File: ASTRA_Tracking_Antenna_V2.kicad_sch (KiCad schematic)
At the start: 23 parts, among them J2 24V, J3 24V, J4 24V, J5 5V, J6 Conn_01x04_Socket, M1 Stepper Motor, U4 D24V22F3, U5 D24V22F5

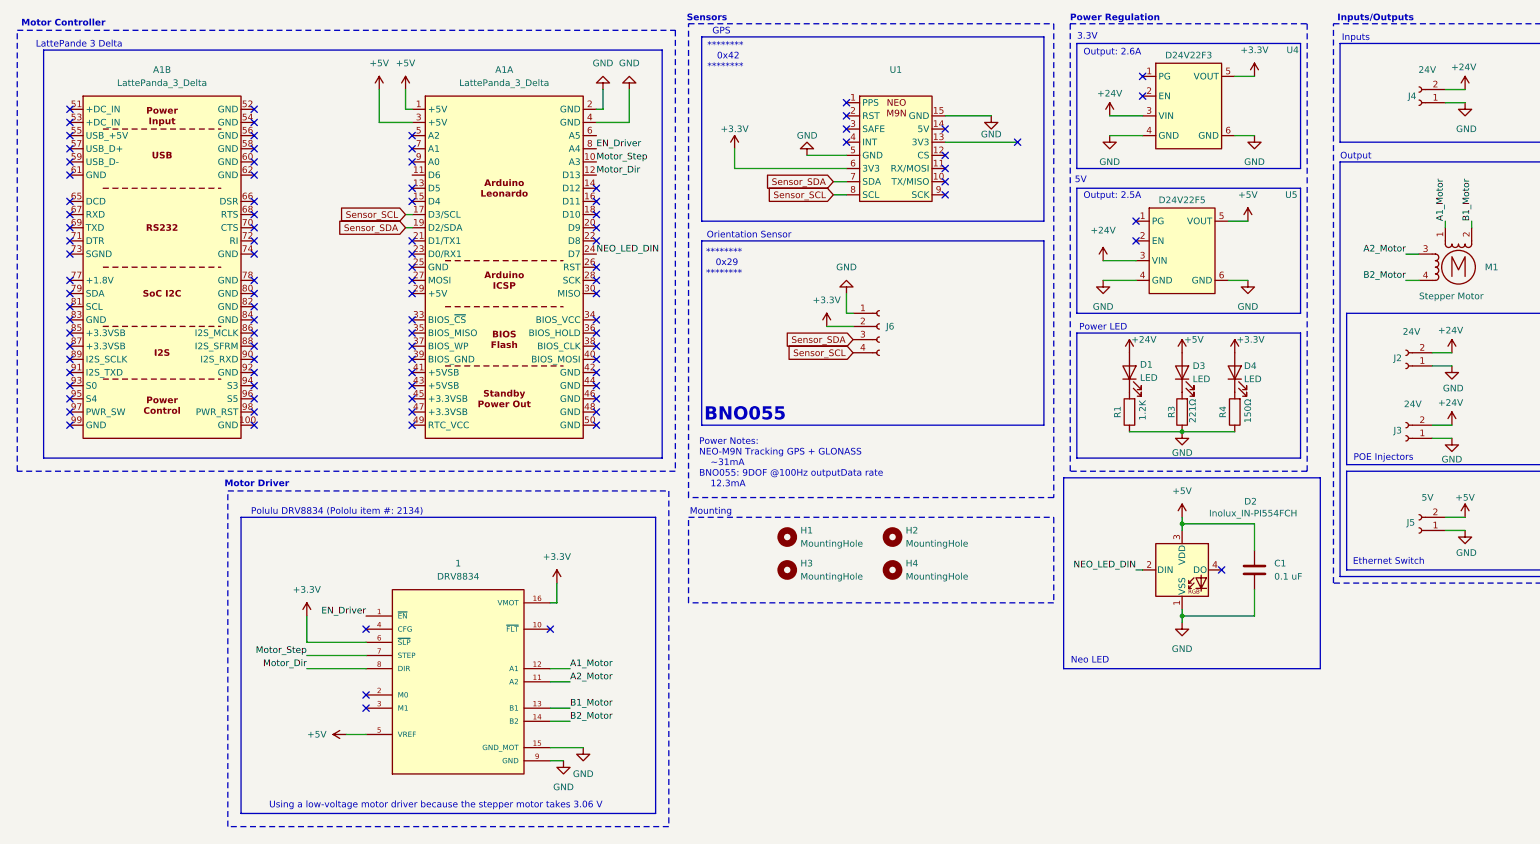
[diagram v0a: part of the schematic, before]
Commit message: PCB Created With SMD Driver
Tracking Antenna PCB revised to incorporate an SMD motor driver, and extraneous files also cleaned up.
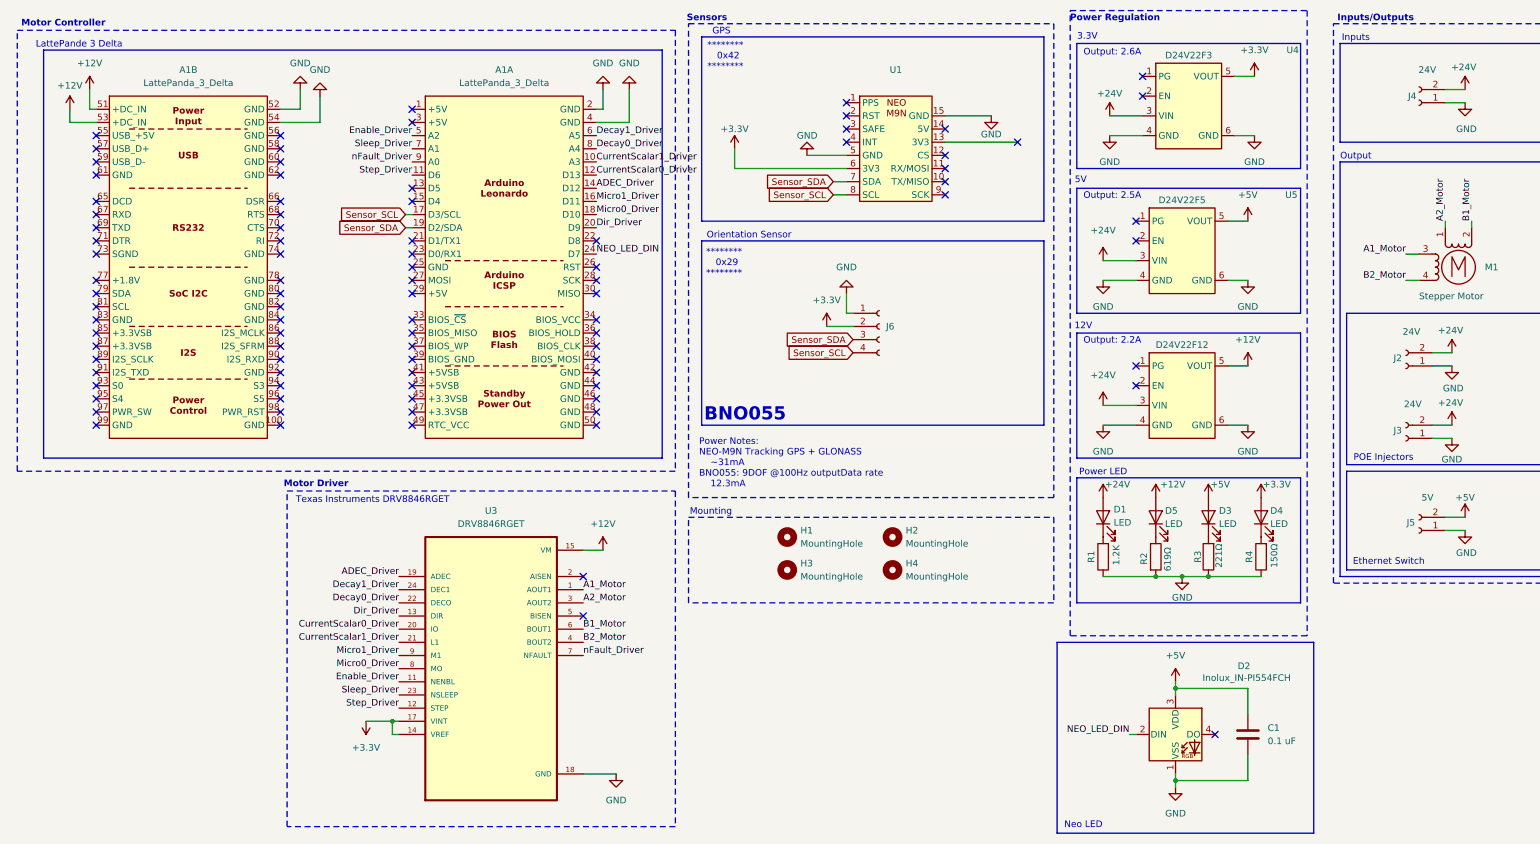
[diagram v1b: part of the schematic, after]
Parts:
- removed 1: DRV8834, Tracking Ant:Polulu_DRV8834, symbol Tracking_Antenna_25_Symbols:DRV8834
- added D5: LED, Tracking Ant:LED 3mm, symbol Device:LED
- added R2: 619Ω, Resistor_SMD:R_0603_1608Metric_Pad0.98x0.95mm_HandSolder, symbol Device:R
- added U2: D24V22F12, Tracking Ant:D24V22Fx, symbol Tracking_Antenna_25_Symbols:D24V22Fx
- added U3: DRV8846RGET, Tracking Ant:DRV8846, symbol Tracking_Antenna_25_Symbols:DRV8846RGET
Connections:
- net +24V: now also U2.3 (VIN)
- net +3.3V: now also U3.14 (VREF), U3.17 (VINT)
- net +5V: no longer A1.1 (+5V), A1.3 (+5V)
- net A1_Motor: now also M1.3, U3.1 (AOUT1); no longer M1.1
- net A2_Motor: now also M1.1, U3.3 (AOUT2); no longer M1.3
- net B1_Motor: now also U3.6 (BOUT1)
- net B2_Motor: now also U3.4 (BOUT2)
- net GND: now also A1.52 (GND), A1.54 (GND), R2.2, U2.4 (GND), U2.6 (GND), U3.18 (GND)
- net +12V: now reaches A1.51 (+DC_IN)
- net +12V: now also A1.53 (+DC_IN), D5.2 (A), U2.5 (VOUT), U3.15 (VM)
- net Step_Driver: now reaches A1.11 (D6)
- net Step_Driver: now also U3.12 (STEP)
- net ADEC_Driver: now reaches A1.14 (D12)
- net ADEC_Driver: now also U3.19 (ADEC)
- net Micro1_Driver: now reaches A1.16 (D11)
- net Micro1_Driver: now also U3.9 (M1)
- net Micro0_Driver: now reaches A1.18 (D10)
- net Micro0_Driver: now also U3.8 (MO)
- net Dir_Driver: now reaches A1.20 (D9)
- net Dir_Driver: now also U3.13 (DIR)
- net Enable_Driver: now reaches A1.5 (A2)
- net Enable_Driver: now also U3.11 (NENBL)
- net Decay1_Driver: now reaches A1.6 (A5)
- net Decay1_Driver: now also U3.24 (DEC1)
- net Sleep_Driver: now reaches A1.7 (A1)
- net Sleep_Driver: now also U3.23 (NSLEEP)
- net nFault_Driver: now reaches A1.9 (A0)
- net nFault_Driver: now also U3.7 (NFAULT)
- net EN_Driver renamed Decay0_Driver
- net Decay0_Driver: now also U3.22 (DECO)
- net Motor_Dir renamed CurrentScalar0_Driver
- net CurrentScalar0_Driver: now also U3.20 (IO)
- net Motor_Step renamed CurrentScalar1_Driver
- net CurrentScalar1_Driver: now also U3.21 (L1)
- new net: D5.1 (K), R2.1
- no-connect marks 101 -> 92
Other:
- note added: "12V"
- note added: "Output: 2.2A"
- note added: "Texas Instruments DRV8846RGET"
- note removed: "Polulu DRV8834 (Pololu item #: 2134)"
- note removed: "Using a low-voltage motor driver because the stepper motor takes 3.06 V"
- moved on the sheet: A1B, C1, D1, D2, D3, D4, R1, R3, R4

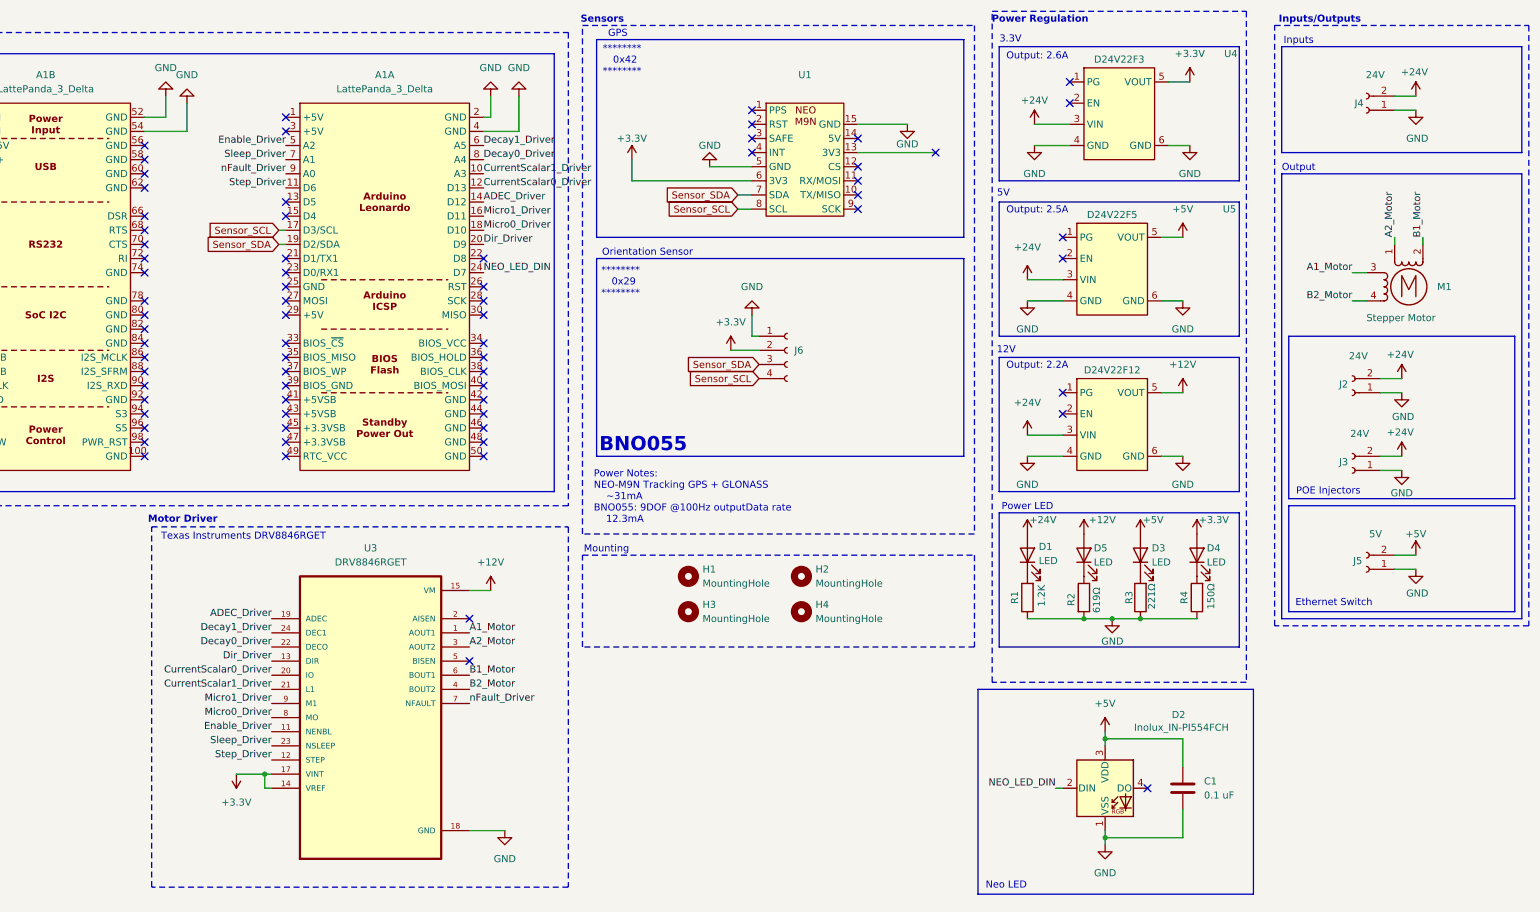
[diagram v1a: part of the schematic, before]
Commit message: PCB Revisions from Feedback and Drone
Revisions made to PCB based on feedback, 3.3V Reg swapped, corrections made to motor driver, connector added for drone subteam.
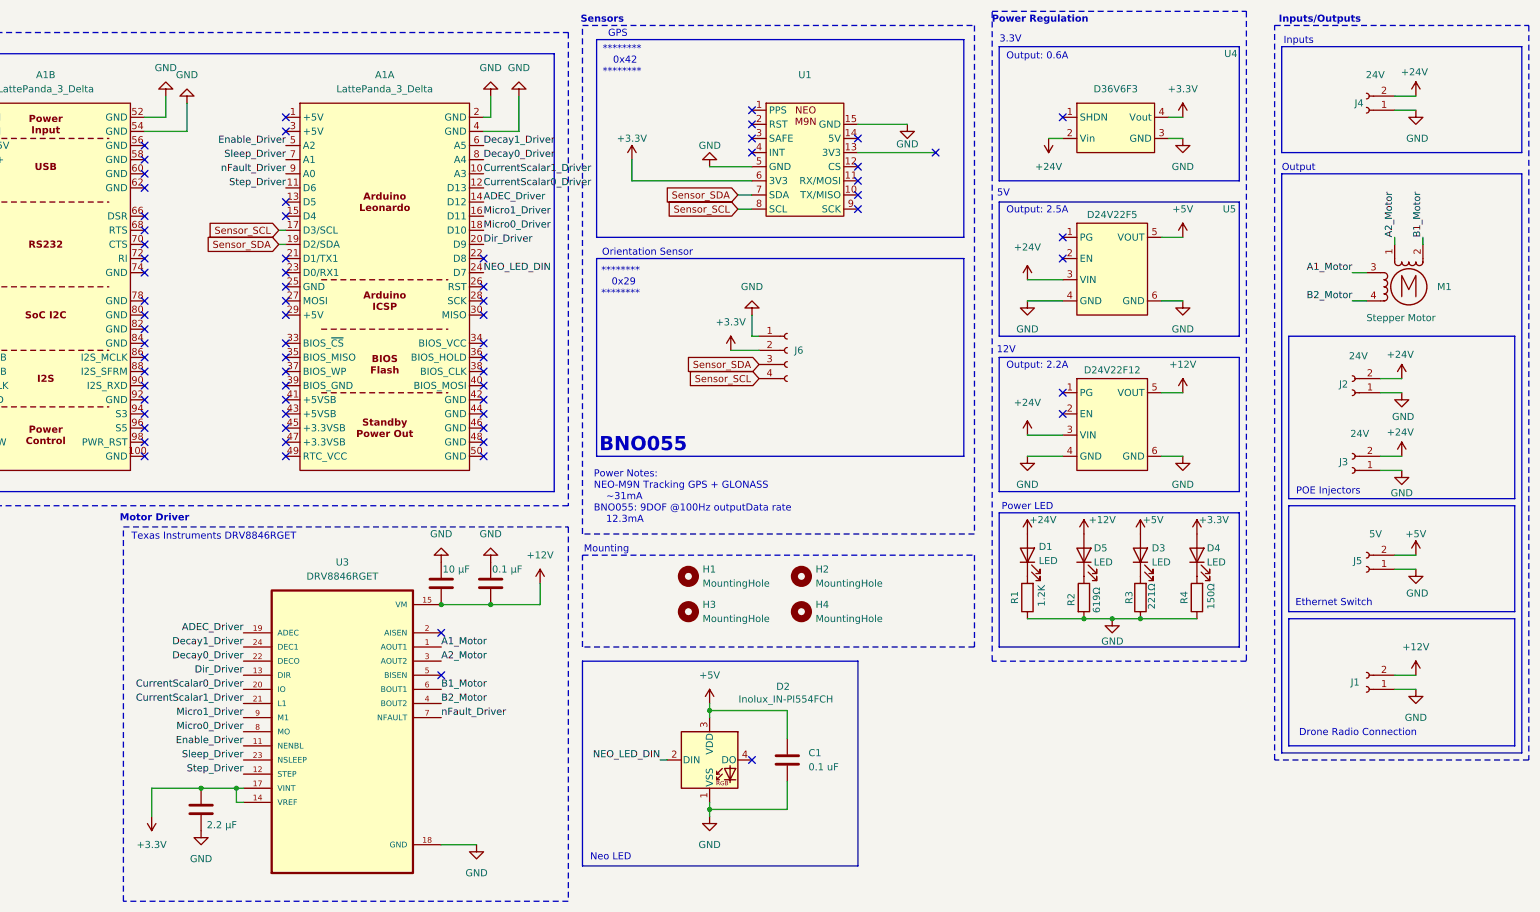
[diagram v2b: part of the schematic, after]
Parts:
- removed U4: D24V22F3, Tracking Ant:D24V22Fx, symbol Tracking_Antenna_25_Symbols:D24V22Fx
- added C2: 2.2 μF, Capacitor_SMD:C_0603_1608Metric_Pad1.08x0.95mm_HandSolder, symbol Device:C
- added C3: 10 μF, Capacitor_SMD:C_0603_1608Metric_Pad1.08x0.95mm_HandSolder, symbol Device:C
- added C4: 0.1 μF, Capacitor_SMD:C_0603_1608Metric_Pad1.08x0.95mm_HandSolder, symbol Device:C
- added J1: Conn_01x02_Socket, Tracking Ant:XT30F_MODIFIED, symbol Connector:Conn_01x02_Socket
- added U4: D36V6F3, Tracking Ant:D36V6F3 3.3V, symbol Tracking_Antenna_25_Symbols:D36V6F3_3.3V
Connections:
- net +12V: now also C3.2, C4.2, J1.2 (Pin_2)
- net +24V: now also U4.2 (Vin)
- net +3.3V: now also C2.1, U4.4 (Vout)
- net GND: now also C2.2, C3.1, C4.1, J1.1 (Pin_1), U4.3 (GND)
- no-connect marks 92 -> 91
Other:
- note added: "Drone Radio Connection"
- note added: "Output: 0.6A"
- note removed: "Output: 2.6A"
- moved on the sheet: C1, D2, U3

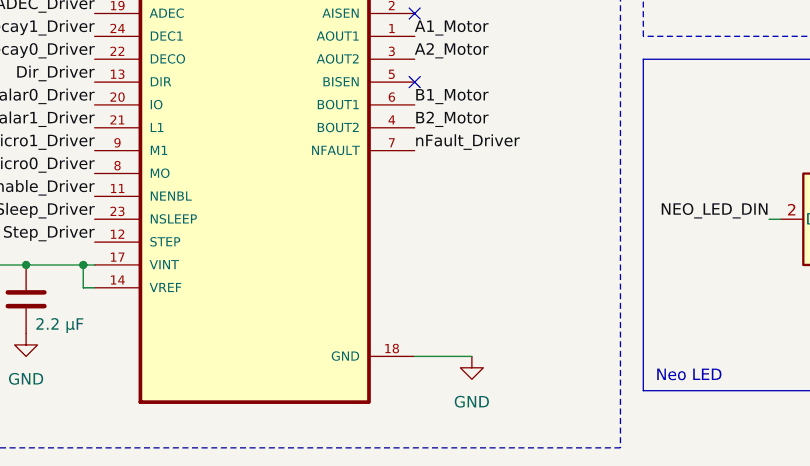
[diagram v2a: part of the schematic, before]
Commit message: Final Tracking Antenna V2
Tracking Antenna final revisions, PCB ordered, drill and gerber files included.
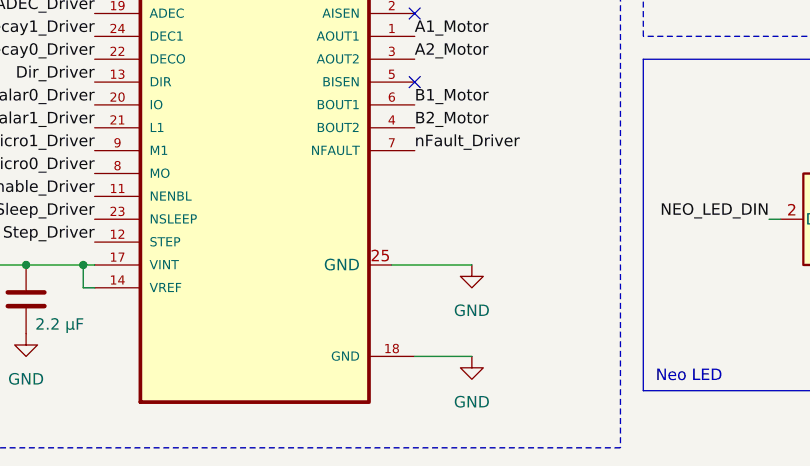
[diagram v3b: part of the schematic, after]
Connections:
- net GND: now also U3.25 (GND)
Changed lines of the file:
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@@
 	(wire
 		(pts
+			(xy 138.43 152.4) (xy 129.54 152.4)
+		)
+		(stroke
+			(width 0)
+			(type default)
+		)
+	)
+	(wire
+		(pts
 			(xy 257.81 121.92) (xy 252.73 121.92)
 		)
@@
 	(symbol
 		(lib_id "power:GND")
+		(at 138.43 152.4 0)
+		(unit 1)
+		(exclude_from_sim no)
+		(in_bom yes)
+		(on_board yes)
+		(dnp no)
+		(fields_autoplaced yes)
+		(property "Reference" "#PWR043"
+			(at 138.43 158.75 0)
+			(effects
+				(font
+					(size 1.27 1.27)
+				)
+				(hide yes)
+			)
+		)
+		(property "Value" "GND"
+			(at 138.43 157.48 0)
+			(effects
+				(font
+					(size 1.27 1.27)
+				)
+			)
+		)
+		(property "Footprint" ""
+			(at 138.43 152.4 0)
+			(effects
+				(font
+					(size 1.27 1.27)
+				)
+				(hide yes)
+			)
+		)
+		(property "Datasheet" ""
+			(at 138.43 152.4 0)
+			(effects
+				(font
+					(size 1.27 1.27)
+				)
+				(hide yes)
+			)
+		)
+		(property "Description" "Power symbol creates a global label with name \"GND\" , ground"
+			(at 138.43 152.4 0)
+			(effects
+				(font
+					(size 1.27 1.27)
+				)
+				(hide yes)
+			)
+		)
+		(pin "1"
+		)
+		(instances
+			(project ""
+				(path "/34f22acd-658e-41b6-b350-204d4a900cb5"
+					(reference "#PWR043")
+					(unit 1)
+				)
+			)
+		)
+	)
+	(symbol
+		(lib_id "power:GND")
 		(at 215.9 33.02 0)
 		(unit 1)
@@
 		(pin "6"
 		)
+		(pin "25"
+		)
 		(instances

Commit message: Tracking Antenna V3
Tracking Antenna PCB has been revised to orient the LattePanda appropriately and replace previous power regulation system with SMD components
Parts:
- removed U4: D36V6F3, Tracking Ant:D36V6F3 3.3V, symbol Tracking_Antenna_25_Symbols:D36V6F3_3.3V
- removed U5: D24V22F5, Tracking Ant:D24V22Fx, symbol Tracking_Antenna_25_Symbols:D24V22Fx
- added C10, C16: 1uF, Capacitor_SMD:C_0603_1608Metric, symbol Device:C_Small
- added C11, C5: 10uF, Capacitor_SMD:C_0603_1608Metric_Pad1.08x0.95mm_HandSolder, symbol Device:C_Small
- added C12, C6: 100nF, Capacitor_SMD:C_0603_1608Metric, symbol Device:C_Small
- added C13, C14, C7, C8: 22uF, Capacitor_SMD:C_0603_1608Metric_Pad1.08x0.95mm_HandSolder, symbol Device:C_Small
- added C15, C9: 4u7F, Capacitor_SMD:C_0603_1608Metric, symbol Device:C_Small
- added JP1: SolderJumper_3_Open, Jumper:SolderJumper-3_P2.0mm_Open_TrianglePad1.0x1.5mm_NumberLabels, symbol Jumper:SolderJumper_3_Open
- added L1, L2: 4u7H, Tracking Ant:WE-MAPI_4030, symbol Device:L
- added U4: AP63203WU-7, Tracking Ant:SOT95P280X100-6N, symbol Cosmos Schematic Symbols:AP63203WU-7
- added U5: AP63205WU-7, Tracking Ant:SOT95P280X100-6N, symbol Cosmos Schematic Symbols:AP63205WU-7
- added U6: ~, Tracking Ant:esp32_devkit_v1, symbol Tracking_Antenna_25_Symbols:ESP32_DOIT_devkit_V1
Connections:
- net +24V: now also C11.1, C5.1, JP1.1 (A), U4.2 (EN), U4.3 (VIN), U5.3 (VIN)
- net +3.3V: now also C10.1, C7.1, C8.1, C9.1, L1.1, U4.1 (FB), U6.1 (ENABLE), U6.16 (3.3V)
- net +5V: now also C13.1, C14.1, C15.1, C16.1, L2.1, U5.1 (FB), U6.15 (VIN)
- net A2_Motor: now also M1.4; no longer M1.1
- net ADEC_Driver: now also U6.11 (GPIO14/A16); no longer A1.14 (D12)
- net B2_Motor: now also M1.1; no longer M1.4
- net CurrentScalar0_Driver: now also U6.10 (GPIO27/A17); no longer A1.12 (D13)
- net CurrentScalar1_Driver: now also U6.9 (GPIO26/A19); no longer A1.10 (A3)
- net Decay0_Driver: now also U6.8 (GPIO25/A18); no longer A1.8 (A4)
- net Decay1_Driver: now also U6.6 (GPIO32/A4); no longer A1.6 (A5)
- net Dir_Driver: now also U6.21 (GPIO16/RX2); no longer A1.20 (D9)
- net Enable_Driver: now also U6.23 (GPIO05/CS); no longer A1.5 (A2)
- net GND: now also C10.2, C11.2, C13.2, C14.2, C15.2, C16.2, C5.2, C7.2, C8.2, C9.2, U4.4 (GND), U5.4 (GND), U6.14 (GND), U6.17 (GND)
- net Micro0_Driver: now also U6.27 (GPIO3/RX0); no longer A1.18 (D10)
- net Micro1_Driver: now also U6.24 (GPIO18/SCK); no longer A1.16 (D11)
- net NEO_LED_DIN: now also U6.12 (GPIO12/A15); no longer A1.24 (D7)
- net Sensor_SCL: now also U6.29 (GPIO22/SCL); no longer A1.17 (D3/SCL)
- net Sensor_SDA: now also U6.26 (GPIO21/SDA); no longer A1.19 (D2/SDA)
- net Sleep_Driver: now also U6.7 (GPIO33/A5); no longer A1.7 (A1)
- net Step_Driver: now also U6.22 (GPIO17/TX2); no longer A1.11 (D6)
- net nFault_Driver: now also U6.28 (GPIO1/TX0); no longer A1.9 (A0)
- new net: C6.2, L1.2, U4.5 (SW)
- new net: C6.1, U4.6 (BST)
- new net: C12.2, L2.2, U5.5 (SW)
- new net: C12.1, U5.6 (BST)
- new net: JP1.2 (C), U5.2 (EN)
- new net 5VREG_EN: JP1.3 (B), U6.20 (GPIO4/A10)
- no-connect marks 91 -> 112
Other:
- note added: "ESP32"
- note removed: "Output: 0.6A"
- note removed: "Output: 2.5A"
- moved on the sheet: D1, D3, D4, D5, J1, J2, J3, J4, J5, M1, R1, R2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
